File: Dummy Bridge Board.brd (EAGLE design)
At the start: 100 x 80 mm, 90 parts, among them J2 5787834-1, U14 ADUM3160BRWZ-RL, U22 PDS1-S5-S5-M-TR, U28 FT4232HL, U29 SN74HC595DR, U30 LP5907MFX-3.3/NOPB, U9 TPS54540DDARQ1, Y2 CX3225GB12000P0HPQCC

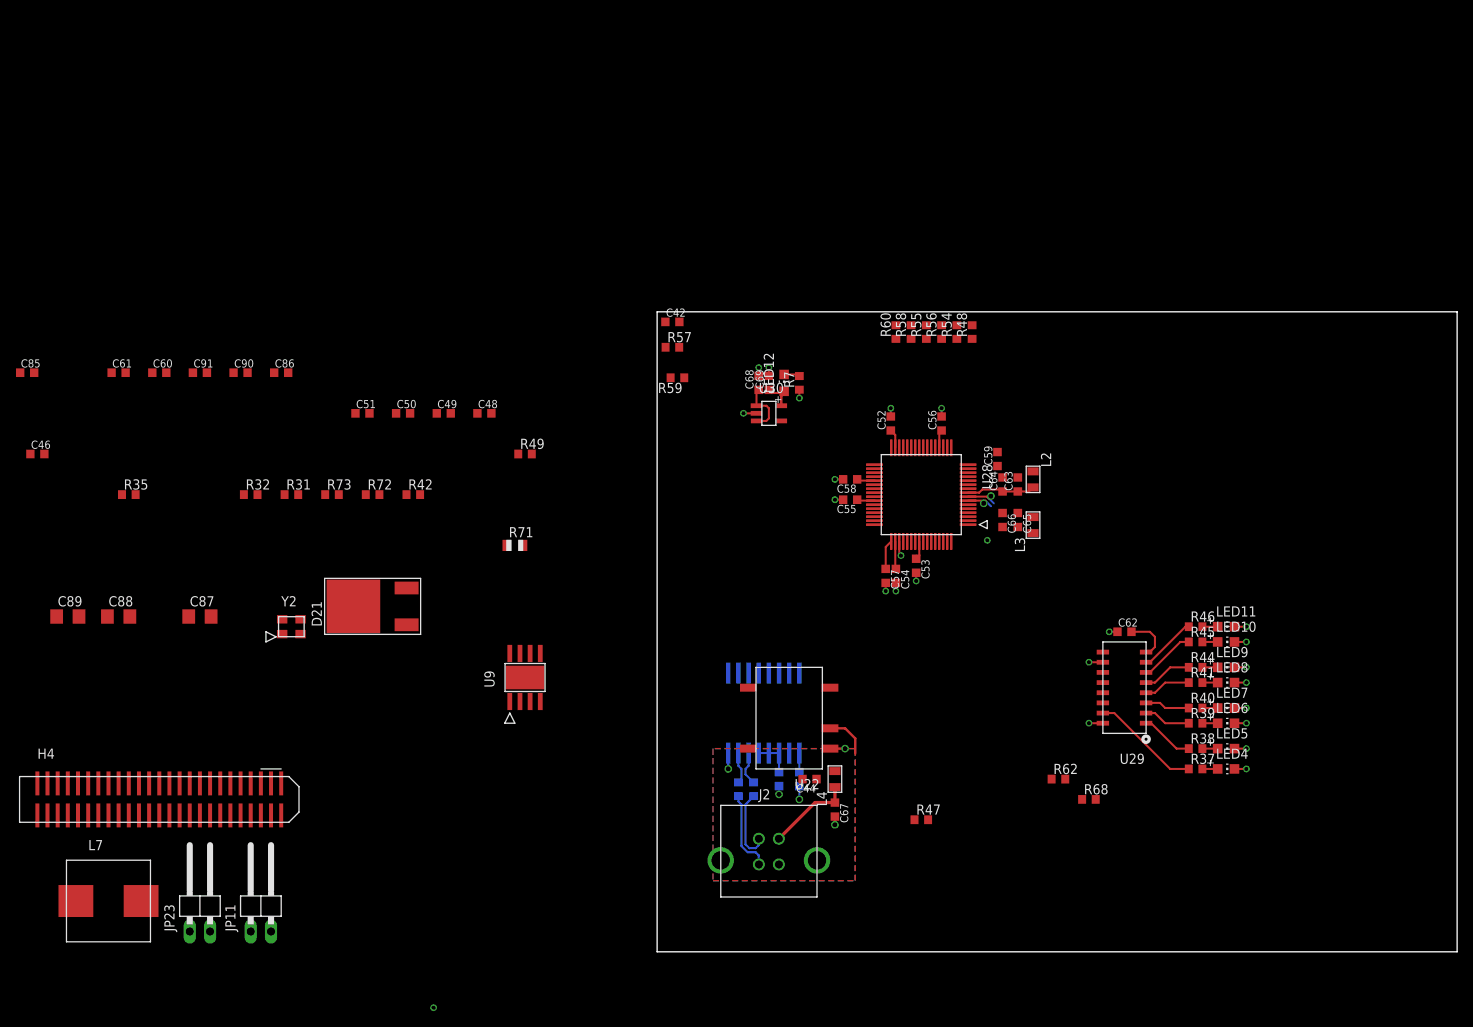
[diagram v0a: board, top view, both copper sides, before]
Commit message: DONE- added vert banana sockets
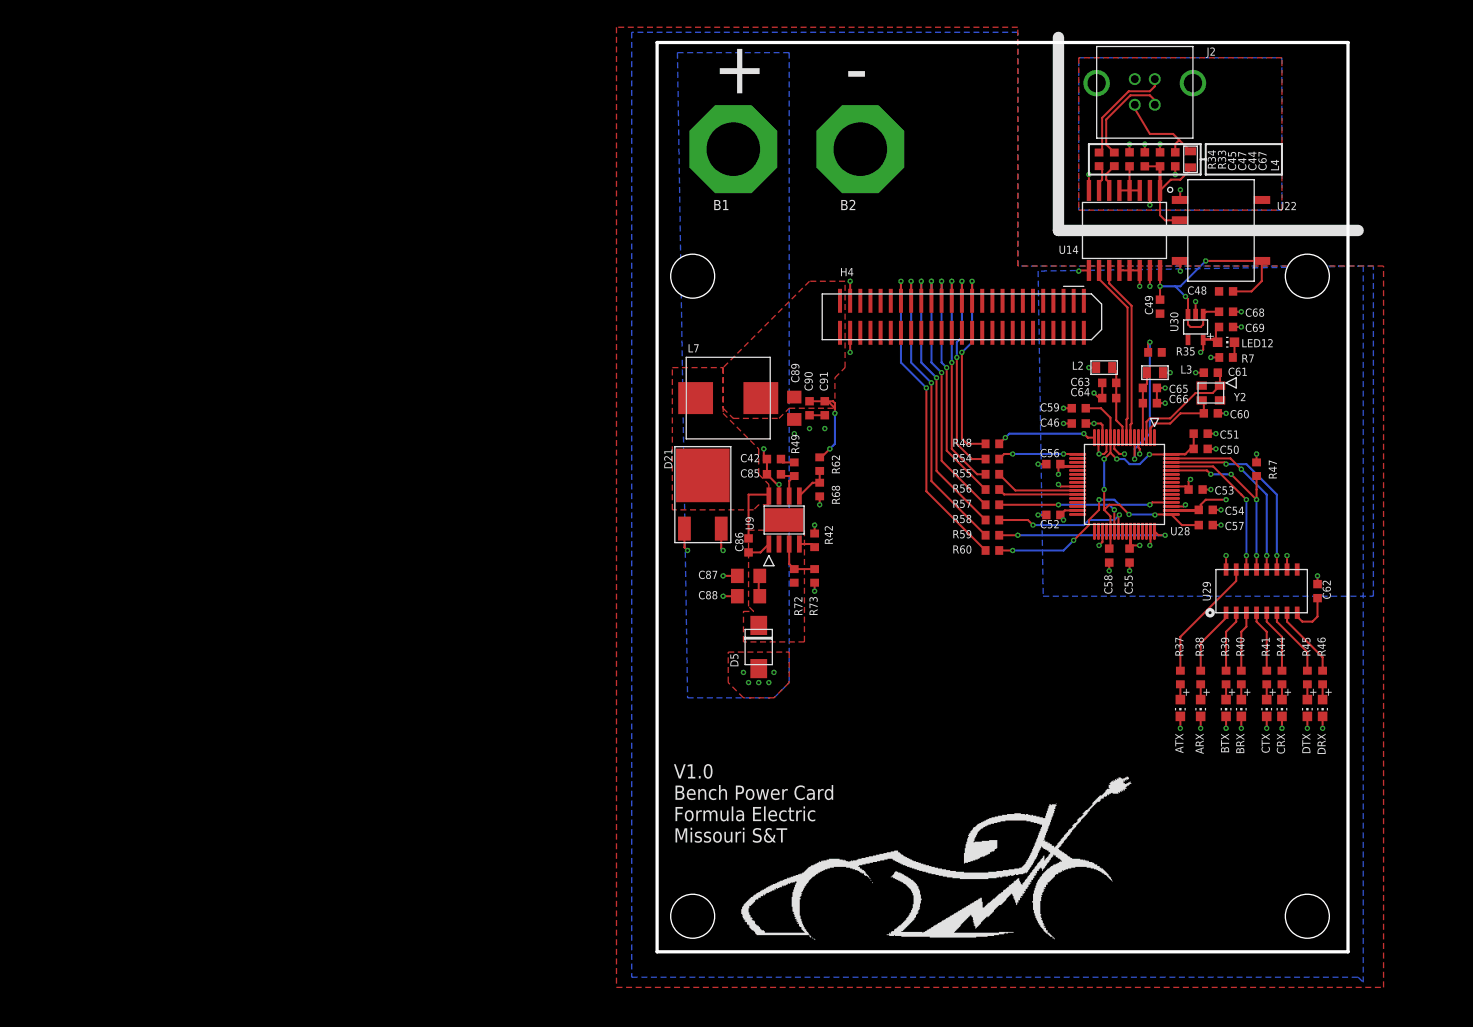
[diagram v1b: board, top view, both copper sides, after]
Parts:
- removed H1: 0.1" Jumper, FormE:EMPTY_FOOTPRINT
- removed JP11, JP23: (no value), pinhead:1X02/90
- removed LED10, LED11, LED4, LED5, LED6, LED8, LED9: ORANGE, FormE:CHIP-LED0805
- removed R31, R32: 1k, rcl:R0603
- removed R71: 0.007, adafruit:R0805
- added ARX, ATX, BRX, CRX, CTX, DRX, DTX: ORANGE, FormE:CHIP-LED0805
- added B1: BKCT2228-2-ND, FormE:BANANA_SOCKET_VERT
- added B2: BKCT2228-0-ND, FormE:BANANA_SOCKET_VERT
- added D5: PMEG3030EP,115, FormE:SOD-128
- added H2: CARCONTROLLER-REF, FormE:CARCONTROLLER-REF
- moved C61 136.5 mm to (69.2, 72.4), turned to 180 degrees
- moved C60 131.5 mm to (69.2, 67.3)
- moved C46 130.2 mm to (52.7, 66.0), turned to 180 degrees
- moved R35 129.5 mm to (62.2, 74.9), turned to 180 degrees
- moved Y2 118.6 mm to (69.2, 69.8), turned to 180 degrees
- moved H4 117.1 mm to (38.1, 79.4)
- moved J2 107.9 mm to (61.0, 108.6), turned to 180 degrees
- moved C51 104.8 mm to (67.9, 64.8)
- moved C50 99.8 mm to (67.9, 62.9)
- moved L7 99.8 mm to (8.89, 69.2)
- moved C89 94.5 mm to (17.1, 67.9), turned to 270 degrees
- moved C85 94.2 mm to (14.6, 59.7), turned to 180 degrees
- moved C48 94.0 mm to (71.1, 82.5), turned to 180 degrees
- moved C67 91.7 mm to (64.8, 99.1)
- moved R33 90.7 mm to (57.1, 99.1), flipped to the top, turned to 270 degrees
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- renumbered LED7 to BTX
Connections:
- removed net !PD: H4.46
- removed net !POR: H4.44
- removed net 5V_CURRENT_SENSE+: C89.1, C90.1, C91.1, L7.P$2, R71.1
- removed net 5V_CURRENT_SENSE-: JP11.1, R62.2, R71.2
- removed net N$16: JP23.1, R32.2
- removed net N$6: JP23.2, R31.2
- new net N$2: B1.P$1, D5.ANODE
- net +5V: now also C89.1, C90.1, C91.1, L7.P$2, R62.2; no longer JP11.2
- net GND: now also ARX.C, ATX.C, B2.P$1, BRX.C, CRX.C, CTX.C, DRX.C, DTX.C; no longer LED10.C, LED11.C, LED4.C, LED5.C, LED6.C, LED8.C, LED9.C
- net N$63: now also ATX.A; no longer LED4.A
- net N$64: now also ARX.A; no longer LED5.A
- net N$65: now also BTX.A; no longer LED6.A
- net N$66: now also BRX.A; no longer BTX.A
- net N$67: now also CTX.A; no longer LED8.A
- net N$68: now also CRX.A; no longer LED9.A
- net N$69: now also DTX.A; no longer LED10.A
- net N$70: now also DRX.A; no longer LED11.A
- net UART_RX1: now also H4.28; no longer R31.1
- net UART_TX1: now also H4.26; no longer R32.1
- net VCC: now also D5.CATHODE
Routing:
- net GND: track 31.7 -> 92.3 mm, vias 20 -> 52
- net VCORE: track 5.95 -> 49.6 mm, vias 0 -> 6
- net UART_TX4: track 0.00 -> 40.5 mm, vias 0 -> 2
- net UART_RX4: track 0.00 -> 38.1 mm, vias 0 -> 2
- net UART_TX3: track 0.00 -> 35.6 mm, vias 0 -> 2
- net UART_RX3: track 0.00 -> 33.2 mm, vias 0 -> 2
- net UART_TX2: track 0.00 -> 30.8 mm, vias 0 -> 2
- net VCCIO: track 23.6 -> 53.8 mm, vias 3 -> 14
- net UART_RX2: track 0.00 -> 29.7 mm, vias 0 -> 2
- net +5V/1: track 6.73 -> 35.3 mm, vias 0 -> 3
- net UART_TX1: track 0.00 -> 27.4 mm, vias 0 -> 2
- net UART_RX1: track 0.00 -> 25.9 mm, vias 0 -> 2
- net RXD_D: track 0.00 -> 25.6 mm, vias 0 -> 4
- net EECLK: track 0.00 -> 24.2 mm, vias 0 -> 2
- net !PWREN!: track 0.00 -> 23.9 mm, vias 0 -> 4
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- added copper zone on layer 1, net +5V
- added copper zone on layer 1, net GND
- added copper zone on layer 16, net GND
- added copper zone on layer 1, net N$2
- added copper zone on layer 16, net N$2
- added copper zone on layer 1, net SW_5V
- added copper zone on layer 1, net USBISO_GND
- added copper zone on layer 1, net VCC
- added copper zone on layer 16, net VCCIO
- removed copper zone on layer 1, net USBISO_VCC
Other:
- board size 100 x 80 mm -> 86.4 x 113.7 mm
- board text added: "+"
- board text added: "-"
- board text added: "V1.0 Bench Power Card Formula Electric Missouri S&T"

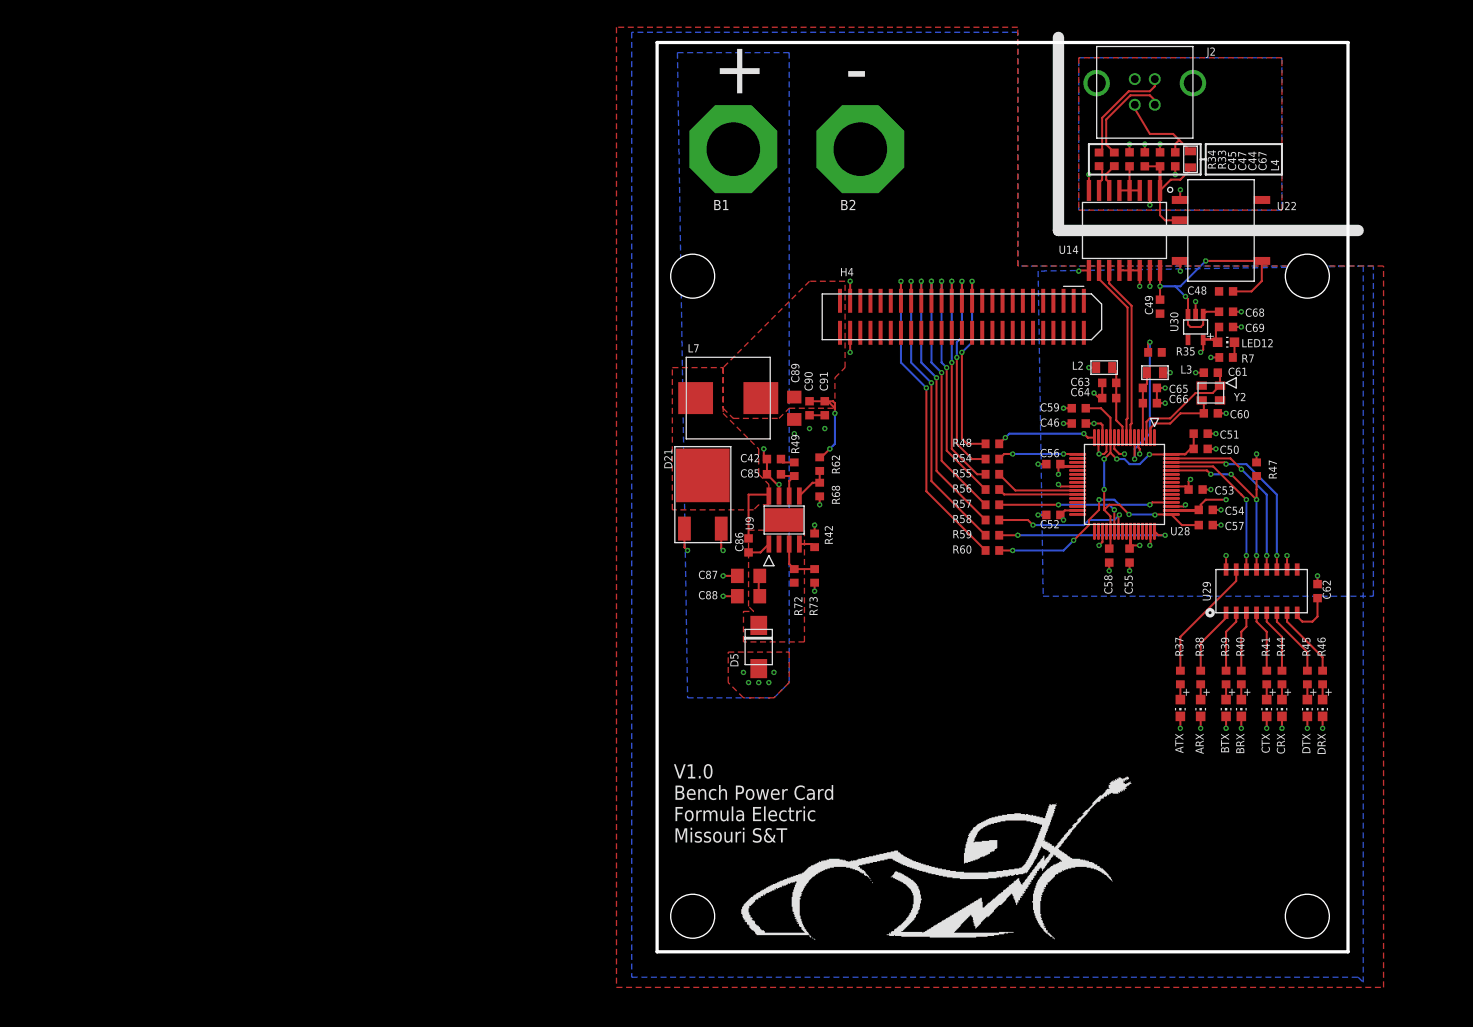
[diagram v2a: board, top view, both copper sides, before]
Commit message: Added Voltage supervisor, about to finish BOM
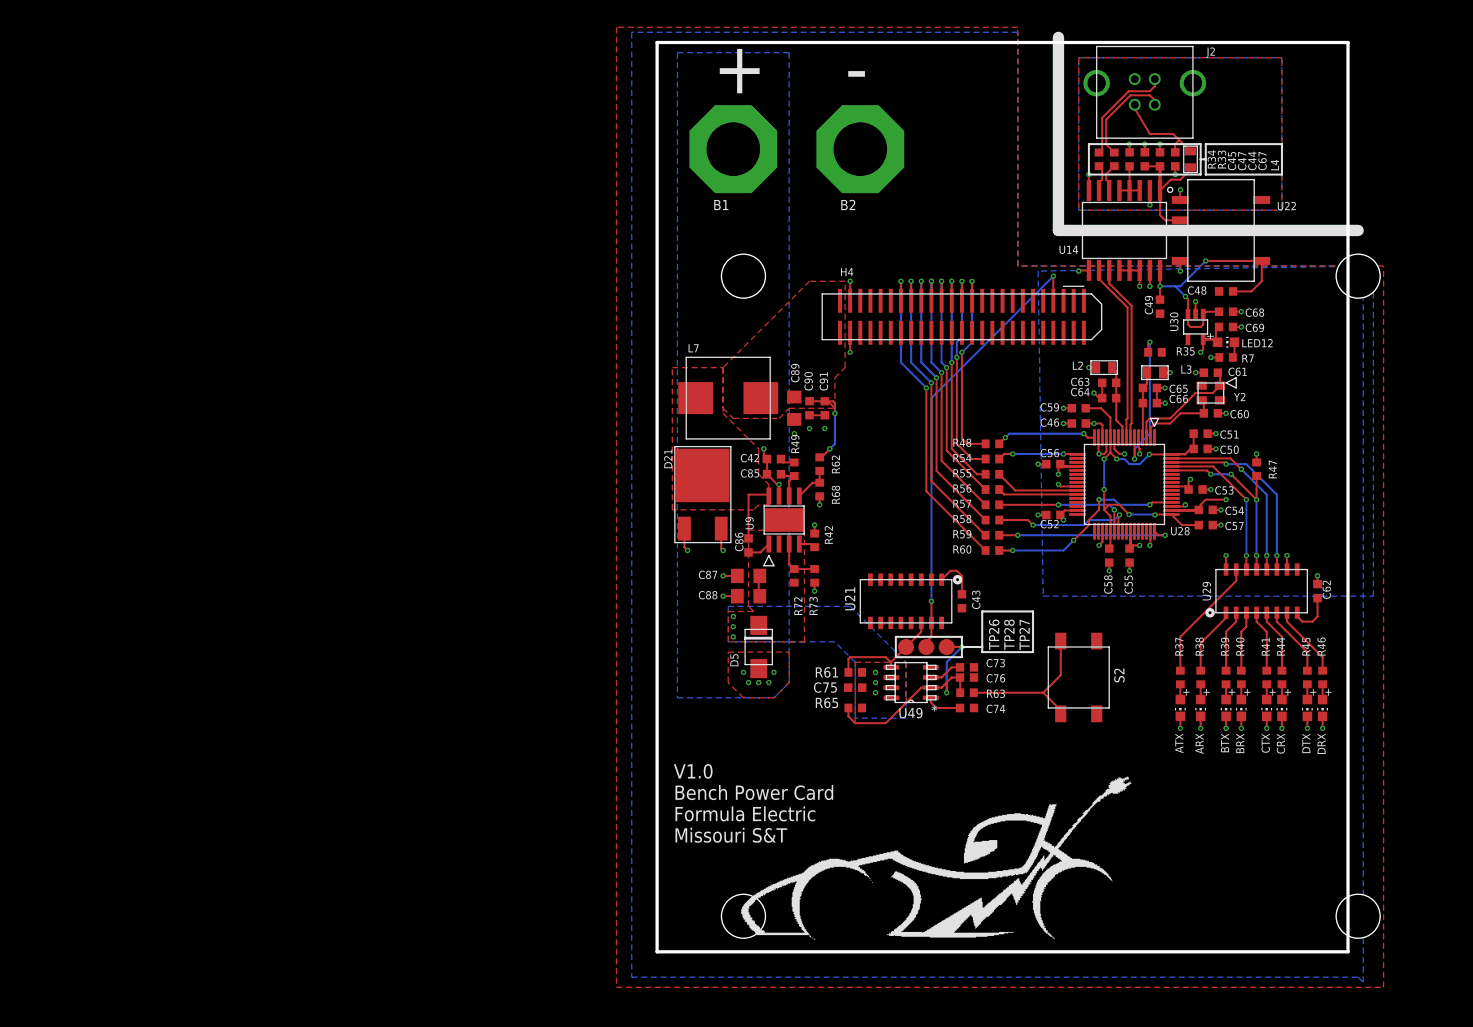
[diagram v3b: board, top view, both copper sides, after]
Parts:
- added C43, C73, C74: 0.1uF, rcl:C0603K
- added C75, C76: 1uF, rcl:C0603K
- added R61, R65: 10k, rcl:R0603
- added R63: 100, rcl:R0603
- added S2: TE-FSM4JSMATR, FormE:TE-FSM4JSMATR
- added TP26, TP27, TP28: PTR1TP20R, testpad:TP20R
- added U21: CD4050BD, FormE:SOIC-16
- added U49: TL7712A-SOIC, FormE:D8
- moved H2 6.35 mm to (54.0, 41.3)
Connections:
- new net !POR: H4.44, TP28.TP, U21.15
- new net +3V3: C43.1, U21.1
- new net MAN_RESET_SIGNAL: C76.1, R63.1, R65.1, TP27.TP, U49.2
- new net N$60: R61.1, TP26.TP, U21.14, U49.5
- new net N$72: C74.1, U49.1
- new net N$73: C73.1, U49.3
- new net N$74: R63.2, S2.1, S2.2
- net GND: now also C43.2, C73.2, C74.2, C75.2, C76.2, S2.3, S2.4, U21.8, U49.4
- net VCC: now also C75.1, R61.2, R65.2, U49.7, U49.8
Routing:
- net !POR: track 0.00 -> 56.0 mm, vias 0 -> 2
- net MAN_RESET_SIGNAL: track 0.00 -> 29.3 mm, vias 0 -> 2
- net N$74: track 0.00 -> 19.6 mm
- net N$60: track 0.00 -> 14.5 mm
- net +3V3: track 0.00 -> 5.56 mm
- net N$72: track 0.00 -> 4.50 mm
- net N$73: track 0.00 -> 4.17 mm
- net VCC: vias 0 -> 6
- added copper zone on layer 16, net VCC

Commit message: BOM Exported and minor board change- ready to order
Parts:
- moved H2 6.35 mm to (47.6, 41.3)
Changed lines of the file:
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@@
 <attribute name="PARTNO" value="CX3225GB12000P0HPQCC" x="69.215" y="69.85" size="1.778" layer="27" rot="R180" display="off"/>
 </element>
-<element name="H2" library="FormE" package="CARCONTROLLER-REF" value="CARCONTROLLER-REF" x="53.975" y="41.275" smashed="yes"/>
+<element name="H2" library="FormE" package="CARCONTROLLER-REF" value="CARCONTROLLER-REF" x="47.625" y="41.275" smashed="yes"/>
 <element name="D5" library="FormE" package="SOD-128" value="PMEG3030EP,115" x="12.7" y="38.1" rot="R90">
 <attribute name="PARTNO" value="PMEG3030EP,115" x="12.7" y="31.115" size="1.016" layer="27" rot="R90" display="off"/>
